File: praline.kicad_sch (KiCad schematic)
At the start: 9 parts, among them J3 RF-SHIELD-FRAME

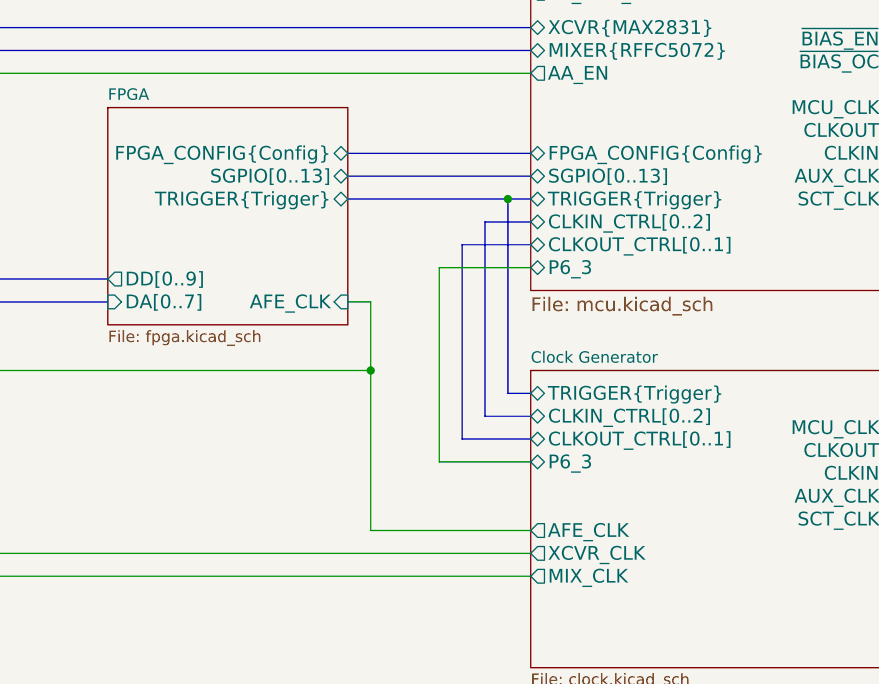
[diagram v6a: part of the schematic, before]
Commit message: Add FPGA_CLK clock generator output
- Remove TRIGGER_EN signal, to be replaced with SPI command
- Reassign clock generator outputs for CLKOUT and CLKIN
- Reassign various FPGA pins
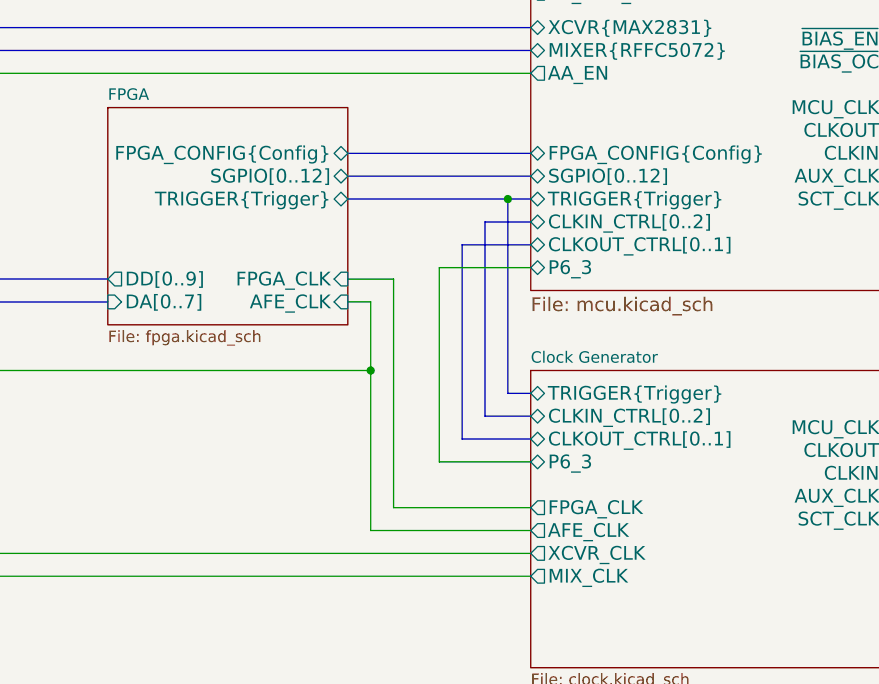
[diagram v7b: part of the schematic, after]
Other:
- sheet Clock Generator ports: added FPGA_CLK; removed none
- sheet FPGA ports: added FPGA_CLK, SGPIO[0..12]; removed SGPIO[0..13]
- sheet Microcontroller ports: added SGPIO[0..12]; removed SGPIO[0..13]
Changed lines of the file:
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@@
+	(wire
+		(pts
+			(xy 170.18 109.22) (xy 185.42 109.22)
+		)
+		(stroke
+			(width 0)
+			(type default)
+		)
+	)
 	(wire
 		(pts
@@
 		)
 	)
+	(wire
+		(pts
+			(xy 170.18 83.82) (xy 170.18 109.22)
+		)
+		(stroke
+			(width 0)
+			(type default)
+		)
+	)
 	(bus
 		(pts
@@
 		(pts
 			(xy 45.72 44.45) (xy 17.78 44.45)
+		)
+		(stroke
+			(width 0)
+			(type default)
+		)
+	)
+	(wire
+		(pts
+			(xy 165.1 83.82) (xy 170.18 83.82)
 		)
 		(stroke
@@
 			)
 		)
-		(pin "SGPIO[0..13]" bidirectional
+		(pin "SGPIO[0..12]" bidirectional
 			(at 185.42 72.39 180)
 			(effects
@@
 			)
 		)
+		(pin "FPGA_CLK" output
+			(at 185.42 109.22 180)
+			(effects
+				(font
+					(size 1.524 1.524)
+				)
+				(justify left)
+			)
+		)
 		(instances
 			(project "praline"
@@
 			)
 		)
-		(pin "SGPIO[0..13]" bidirectional
+		(pin "SGPIO[0..12]" bidirectional
 			(at 165.1 72.39 0)
 			(effects
@@
 			(effects
 				(font
+					(size 1.524 1.524)
+				)
+				(justify right)
+			)
+		)
+		(pin "FPGA_CLK" input
+			(at 165.1 83.82 0)
+			(effects
+				(font

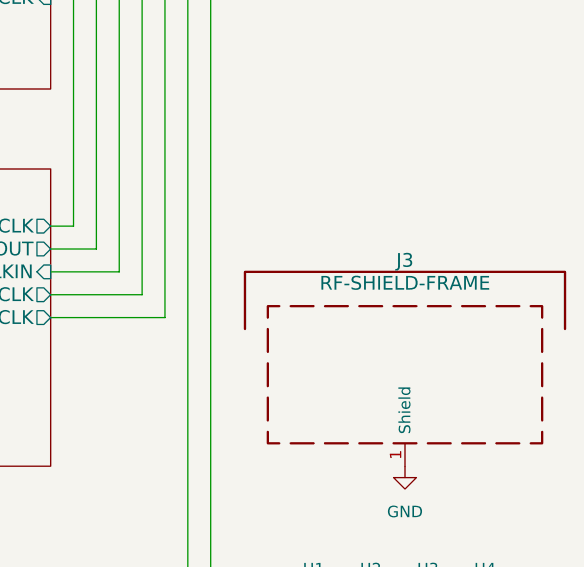
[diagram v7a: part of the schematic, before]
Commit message: Standardize component Value fields
Use Tolerance field instead of expressing tolerance in Value field
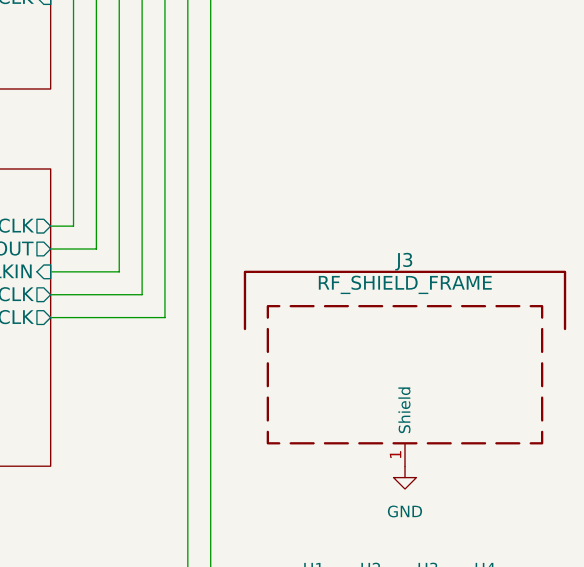
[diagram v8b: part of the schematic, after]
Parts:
- J3: value RF-SHIELD-FRAME -> RF_SHIELD_FRAME
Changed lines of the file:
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@@
 			)
 		)
-		(property "Value" "RF-SHIELD-FRAME"
+		(property "Value" "RF_SHIELD_FRAME"
 			(at 265.43 106.68 0)
 			(effects
